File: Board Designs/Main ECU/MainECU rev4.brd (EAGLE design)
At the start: 120.6 x 78.9 mm, 155 parts, among them Q1 MMBT3904LT3G, Q11 MMBT3904LT3G, Q2 MMBT3904LT3G, Q3 MMBT3904LT3G, Q4 MMBT3904LT3G, Q5 MMBT3904LT3G, Q6 MMBT3904LT3G, Q7 MMBT3904LT3G, Q8 MMBT3904LT3G, Q9 MMBT3904LT3G, X1 CONNECTOR-37, X2 CONNECTOR-4AUTOSPORT, X3 CONNECTOR-4NANO-FIT-VERTICAL-4, X4 CONNECTOR-4NANO-FIT-VERTICAL-4

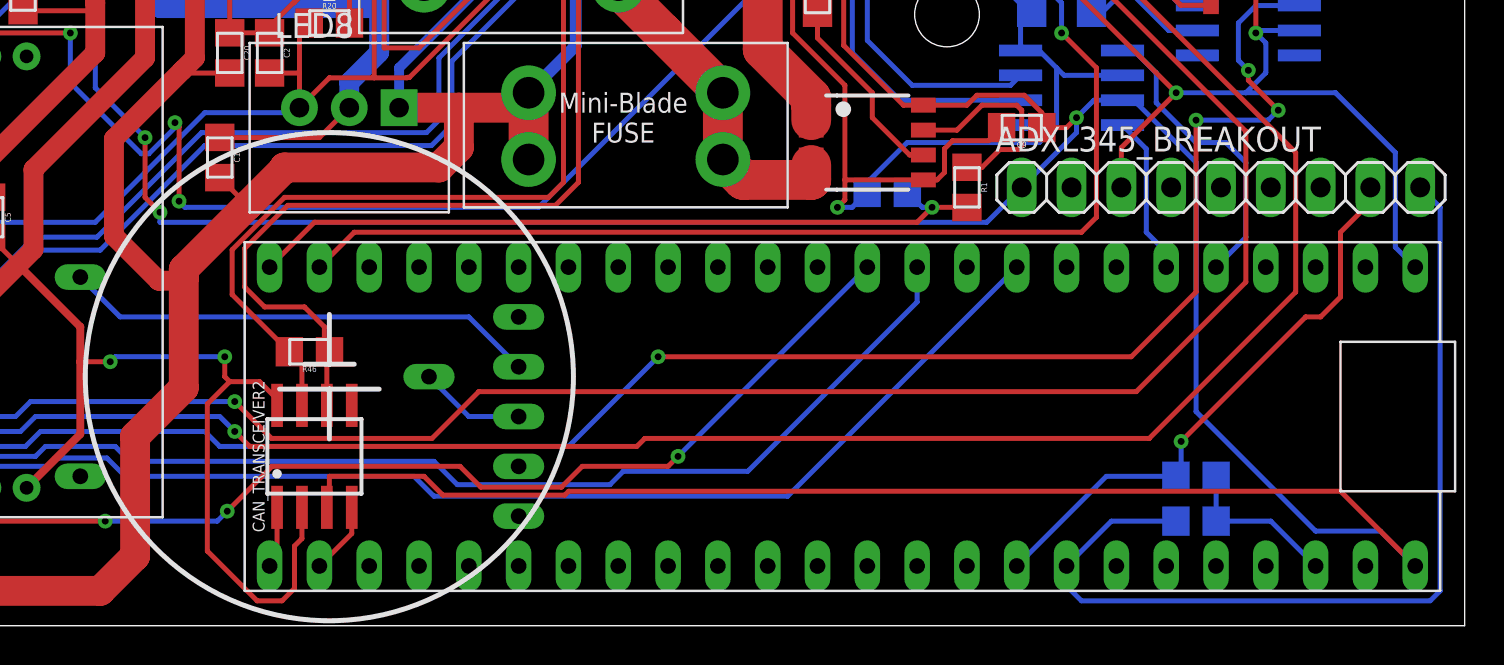
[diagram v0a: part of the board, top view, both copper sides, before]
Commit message: Main ECU rev4: Fixed filter capacitor values again, added filters to current sensor outputs
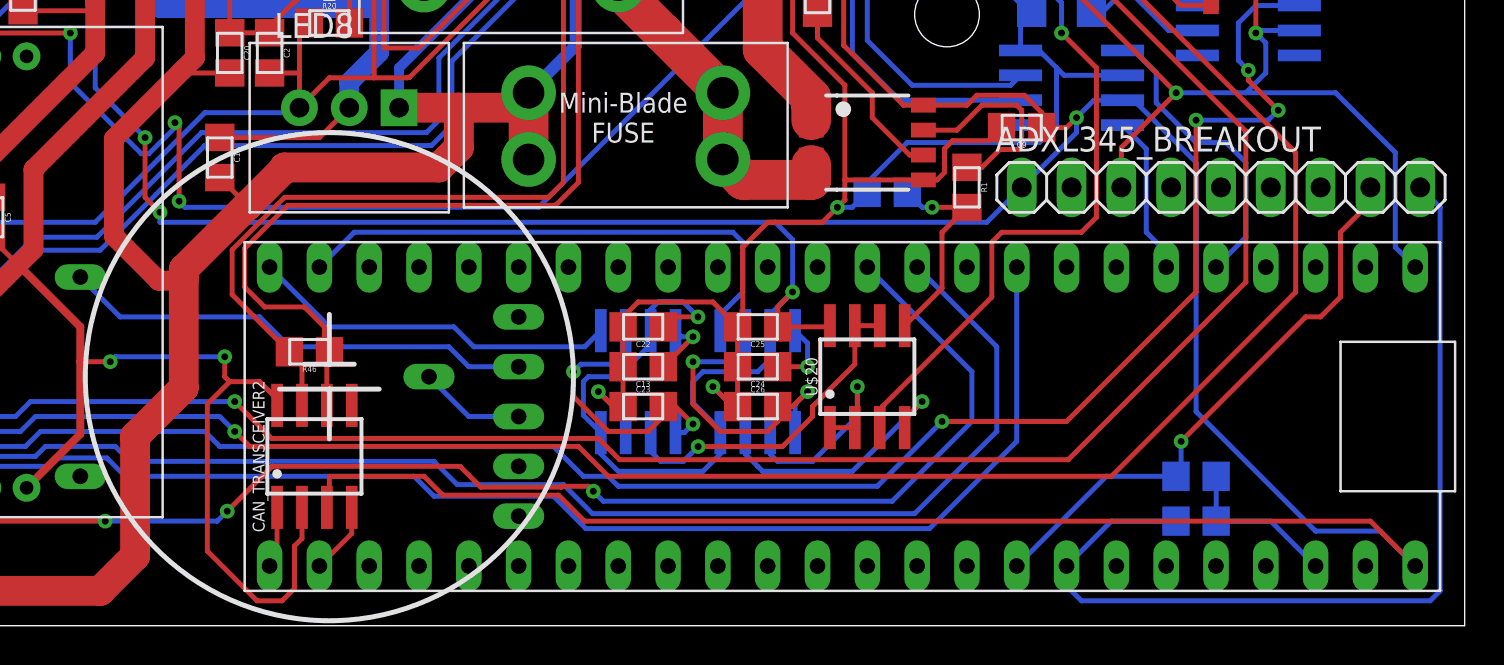
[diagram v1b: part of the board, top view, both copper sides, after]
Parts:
- added C13, C24: 470pF, HyTechDevices:0805
- added C22, C23, C25, C26: .1uF, HyTechDevices:0805
- added U$20: MCP6002SOIC, HyTechDevices:SOIC-08
- added U$21, U$22: (no value), HyTechDevices:SOIC-08
- C14, C17, C3: value 47pF -> 47nF
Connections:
- new net COOLINGSENSE_FILT: U$2.A12, U$22.5
- new net ECUSENSE_FILT: U$2.A13, U$21.5
- new net N$20: U$20.1, U$20.2, U$22.2
- new net N$39: U$20.6, U$20.7, U$21.2
- new net N$43: C23.2, U$21.1, U$21.6
- new net N$44: C13.1, U$21.8
- new net N$67: C26.2, U$22.1, U$22.6
- new net N$68: C24.1, U$22.8
- net COOLINGSENSE: now also U$20.3; no longer U$2.A12
- net ECUSENSE: now also U$20.5; no longer U$2.A13
- net GND: now also C13.2, C22.2, C23.1, C24.2, C25.2, C26.1, U$20.4, U$21.3, U$22.3
- net TELEMETRY5V: now also C22.1, C25.1, U$20.8, U$21.4, U$21.7, U$22.4, U$22.7
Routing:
- net GND: track 774.4 -> 822.2 mm, vias 25 -> 28
- net TELEMETRY5V: track 245.3 -> 288.2 mm, vias 5 -> 7
- net ECUSENSE: track 38.4 -> 10.7 mm
- net COOLINGSENSE_FILT: track 0.00 -> 27.5 mm
- net COOLINGSENSE: track 57.5 -> 34.6 mm
- net ECUSENSE_FILT: track 0.00 -> 18.9 mm
- net N$39: track 0.00 -> 17.2 mm, vias 0 -> 1
- net N$67: track 0.00 -> 16.2 mm, vias 0 -> 2
- net N$43: track 0.00 -> 14.6 mm, vias 0 -> 2
- net XBDI: track 63.8 -> 76.6 mm
- net N$20: track 0.00 -> 11.6 mm, vias 0 -> 1
- net XBDO: track 68.7 -> 79.6 mm
- net XB8: track 68.8 -> 75.3 mm
- net N$68: track 0.00 -> 3.62 mm, vias 0 -> 1
- net N$44: track 0.00 -> 3.17 mm, vias 0 -> 1
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
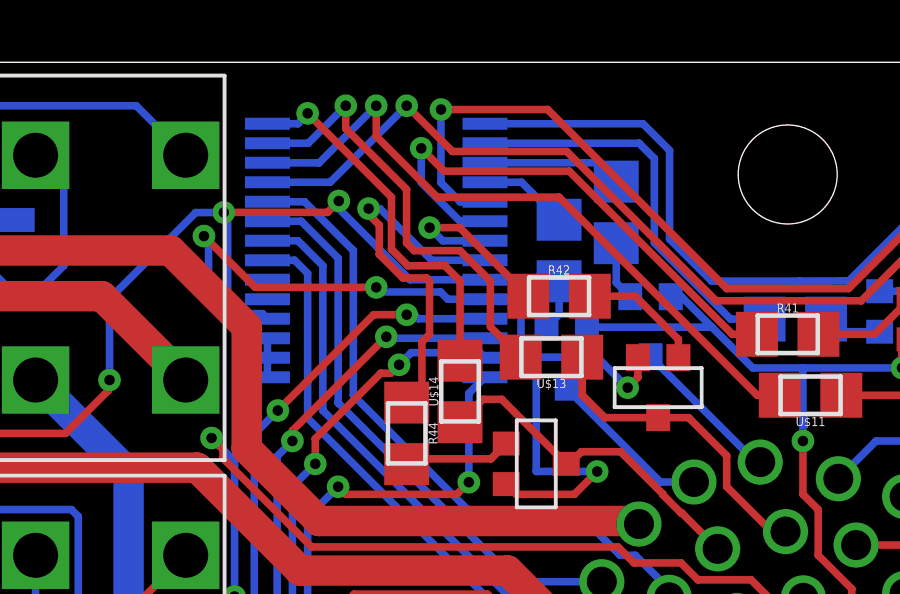
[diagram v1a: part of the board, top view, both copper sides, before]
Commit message: Main ECU rev2/4: Add brake light NPN p/n
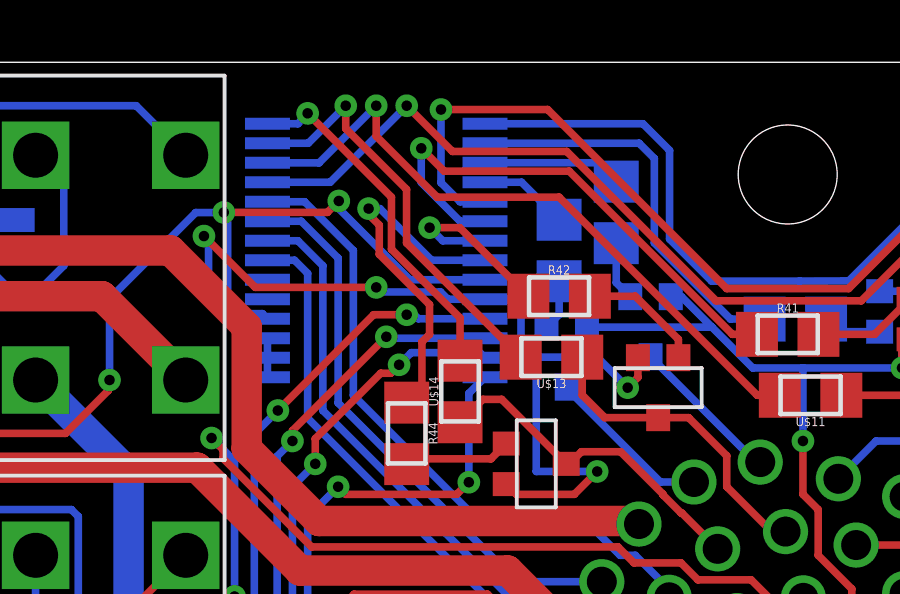
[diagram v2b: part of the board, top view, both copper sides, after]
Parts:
- Q10: value (none) -> MMBT3904LT3G
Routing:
- net DASH_CTRL7_IN: track 14.8 -> 13.9 mm
- net DASH_CTRL8_IN: track 12.6 -> 11.8 mm
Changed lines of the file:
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@@
 <attribute name="VALUE" x="59.6392" y="67.945" size="0.3048" layer="27" rot="R90" align="top-center"/>
 </element>
-<element name="Q10" library="HyTechDevices" package="SOT23" value="" x="59.182" y="49.022" smashed="yes" rot="MR0"/>
+<element name="Q10" library="HyTechDevices" package="SOT23" value="MMBT3904LT3G" x="59.182" y="49.022" smashed="yes" rot="MR0"/>
 <element name="U$15" library="HyTechDevices" package="SOT23" value="BJT_PNPSOT" x="58.928" y="54.61" smashed="yes" rot="MR90"/>
 <element name="R10" library="HyTechDevices" package="0805" value="2.2k" x="64.262" y="46.228" smashed="yes">
@@
 <wire x1="55.88" y1="74.041" x2="56.259" y2="74.041" width="0.254" layer="16"/>
 <wire x1="57.658" y1="69.596" x2="57.658" y2="68.081" width="0.254" layer="1"/>
-<wire x1="57.912" y1="71.628" x2="57.912" y2="69.85" width="0.254" layer="1"/>
 <wire x1="57.912" y1="69.85" x2="57.658" y2="69.596" width="0.254" layer="1"/>
 <wire x1="56.259" y1="74.041" x2="57.981" y2="72.319" width="0.254" layer="16"/>
@@
 <wire x1="55.88" y1="73.8472625" x2="56.2356" y2="73.4916625" width="0.254" layer="1"/>
 <wire x1="56.2356" y1="73.4916625" x2="56.2356" y2="72.51665" width="0.254" layer="1"/>
-<wire x1="56.2356" y1="72.51665" x2="57.02265" y2="71.7296" width="0.254" layer="1"/>
-<wire x1="57.02265" y1="71.7296" x2="57.8104" y2="71.7296" width="0.254" layer="1"/>
-<wire x1="57.8104" y1="71.7296" x2="57.912" y2="71.628" width="0.254" layer="1"/>
 <wire x1="57.981" y1="72.319" x2="59.759" y2="72.319" width="0.254" layer="16"/>
 <wire x1="55.88" y1="74.041" x2="55.88" y2="73.8472625" width="0.254" layer="1"/>
+<wire x1="56.2356" y1="72.51665" x2="57.912" y2="70.84025" width="0.254" layer="1"/>
+<wire x1="57.912" y1="70.84025" x2="57.912" y2="69.85" width="0.254" layer="1"/>
 </signal>
 <signal name="DASH_CTRL7_OUT">
@@
 <contactref element="U$13" pad="2"/>
 <contactref element="U$17" pad="27"/>
-<wire x1="57.1455" y1="72.8935" x2="57.3995" y2="72.6395" width="0.254" layer="1"/>
 <via x="55.118" y="77.47" extent="1-16" drill="0.35"/>
-<wire x1="59.9395" y1="70.0995" x2="60.951" y2="69.088" width="0.254" layer="1"/>
 <wire x1="55.118" y1="77.47" x2="53.867" y2="76.219" width="0.254" layer="16"/>
 <wire x1="53.867" y1="76.219" x2="52.509" y2="76.219" width="0.254" layer="16"/>
 <wire x1="57.1455" y1="74.6805" x2="57.1455" y2="72.8935" width="0.254" layer="1"/>
-<wire x1="57.3995" y1="72.6395" x2="58.928" y2="72.6395" width="0.254" layer="1"/>
 <wire x1="55.118" y1="76.708" x2="57.1455" y2="74.6805" width="0.254" layer="1"/>
 <wire x1="55.118" y1="77.47" x2="55.118" y2="76.708" width="0.254" layer="1"/>
-<wire x1="58.928" y1="72.6395" x2="59.9395" y2="71.628" width="0.254" layer="1"/>
-<wire x1="59.9395" y1="71.628" x2="59.9395" y2="70.0995" width="0.254" layer="1"/>
+<wire x1="57.1455" y1="72.8935" x2="60.951" y2="69.088" width="0.254" layer="1"/>
 </signal>
 <signal name="DASH_CTRL6_IN">
@@
 <via x="53.848" y="77.216" extent="1-16" drill="0.35"/>
 <wire x1="53.848" y1="77.192" x2="53.525" y2="76.869" width="0.254" layer="16"/>
-<wire x1="56.642" y1="72.6849875" x2="56.642" y2="74.422" width="0.254" layer="1"/>
-<wire x1="57.1909875" y1="72.136" x2="58.42" y2="72.136" width="0.254" layer="1"/>
-<wire x1="57.1909875" y1="72.136" x2="56.642" y2="72.6849875" width="0.254" layer="1"/>
+<wire x1="56.642" y1="74.422" x2="56.642" y2="72.6849875" width="0.254" layer="1"/>
 <wire x1="53.848" y1="77.216" x2="56.642" y2="74.422" width="0.254" layer="1"/>
 <wire x1="53.848" y1="77.216" x2="53.848" y2="77.192" width="0.254" layer="16"/>
 <wire x1="53.525" y1="76.869" x2="52.509" y2="76.869" width="0.254" layer="16"/>
-<wire x1="58.42" y1="72.136" x2="58.928" y2="71.628" width="0.254" layer="1"/>
-<wire x1="58.928" y1="71.628" x2="58.928" y2="68.97" width="0.254" layer="1"/>
+<wire x1="56.642" y1="72.6849875" x2="58.928" y2="70.3989875" width="0.254" layer="1"/>
+<wire x1="58.928" y1="70.3989875" x2="58.928" y2="68.97" width="0.254" layer="1"/>
 </signal>
 <signal name="N$28">

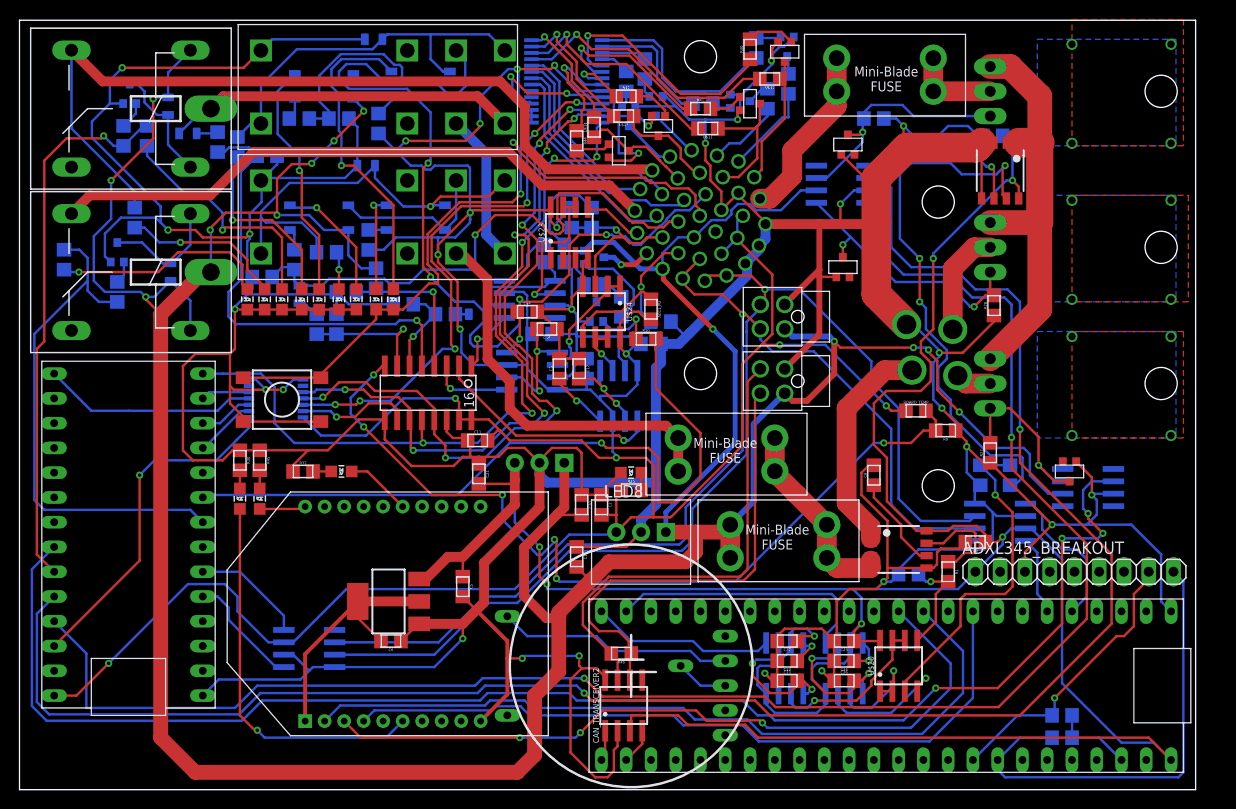
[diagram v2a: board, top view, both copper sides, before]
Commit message: Main ECU rev3/4: Update silkscreen for manufacturing, Main ECU rev4: switch to high-side dashboard switching and flip parts on wrong side
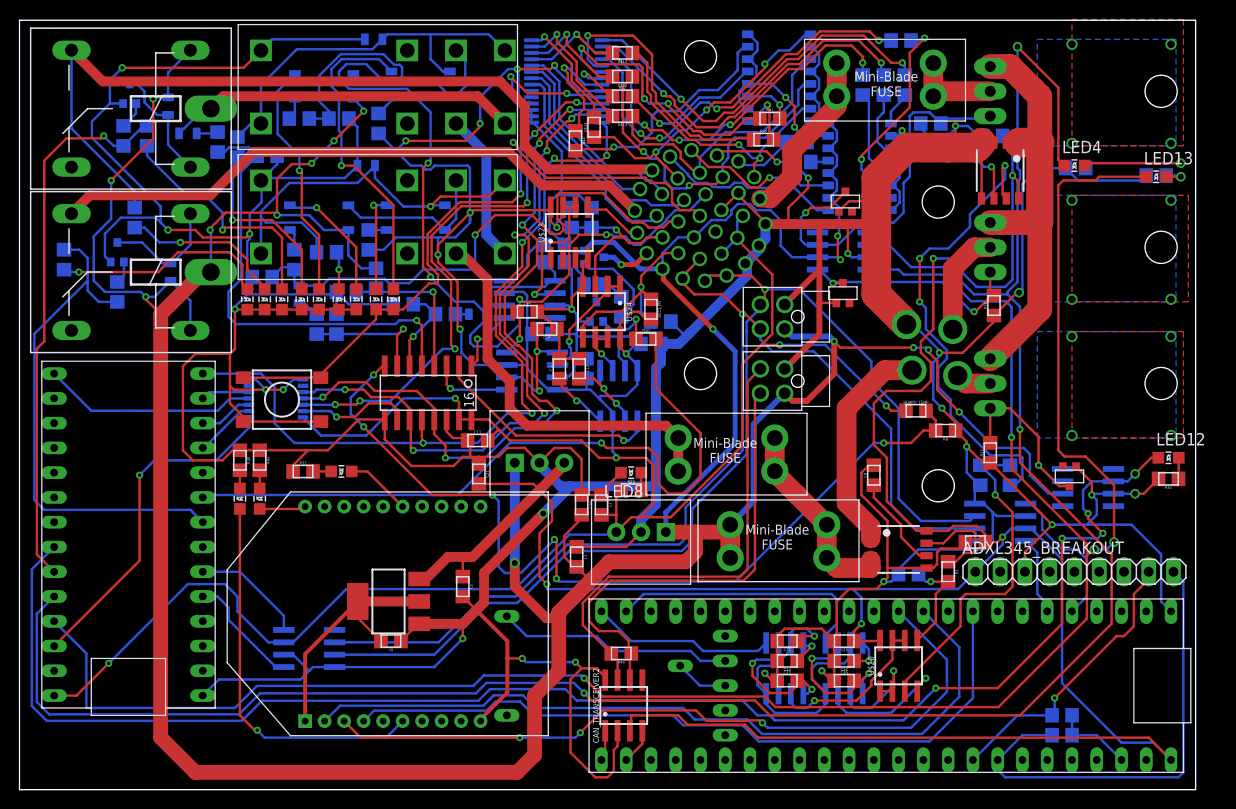
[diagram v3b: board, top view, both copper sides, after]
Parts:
- removed Q1, Q2, Q3, Q4, Q5, Q6, Q7, Q8: MMBT3904LT3G, HyTechDevices:SOT23
- added LED12, LED13, LED4: Red, HyTechDevices:LED-805
- added R25, R51, R52: 100, HyTechDevices:0805
- added U$29, U$30: TLP291-4, HyTechDevices:11-11F1
- moved R39 28.5 mm to (90.4, 76.8), turned to 180 degrees
- moved R38 22.4 mm to (86.5, 72.3)
- moved R36 18.6 mm to (88.6, 72.3), turned to 270 degrees
- moved R35 15.7 mm to (90.8, 72.3), turned to 270 degrees
- moved U$12 15.3 mm to (61.8, 75.6)
- moved U$11 10.3 mm to (61.8, 73.2)
- moved R40 9.38 mm to (76.3, 66.7), turned to 0 degrees
- moved R37 7.33 mm to (80.1, 64.4), turned to 0 degrees
- moved R41 7.18 mm to (77.0, 68.8)
- moved U$5 6.86 mm to (84.5, 55.2)
- moved R43 6.03 mm to (79.8, 66.4), turned to 0 degrees
- moved R24 5.86 mm to (93.5, 68.3), turned to 180 degrees
- moved D8 5.85 mm to (84.7, 60.3)
- moved D7 2.67 mm to (84.5, 50.9)
- moved D9 0.51 mm to (107.7, 32.1)
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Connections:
- new net N$69: LED4.C, R25.1
- new net N$70: LED12.C, R51.1
- new net N$71: LED13.C, R52.1
- net +12V: now also U$29.10, U$29.12, U$29.14, U$29.16, U$30.10, U$30.12, U$30.14, U$30.16
- net DASH_IO3: now also U$29.11; no longer Q3.3
- net DASH_IO4: now also U$29.9; no longer Q4.3
- net DASH_IO5: now also U$30.15; no longer Q5.3
- net DASH_IO6: now also U$30.13; no longer Q6.3
- net DASH_IO7: now also U$30.11; no longer Q7.3
- net DASH_IO8: now also U$30.9; no longer Q8.3
- net FAN1CONTROL: now also LED4.A
- net FAN2CONTROL: now also LED13.A
- net GND: now also R25.2, R51.2, R52.2, U$29.2, U$29.4, U$29.6, U$29.8, U$30.2, U$30.4, U$30.6, U$30.8; no longer Q1.2, Q2.2, Q3.2, Q4.2, Q5.2, Q6.2, Q7.2, Q8.2
- net N$30: now also U$29.3; no longer Q2.1
- net N$42: now also U$29.13; no longer Q2.3
- net N$51: now also U$29.1; no longer Q1.1
- net N$52: now also U$29.5; no longer Q3.1
- net N$53: now also U$29.7; no longer Q4.1
- net N$54: now also U$30.1; no longer Q5.1
- net N$55: now also U$30.3; no longer Q6.1
- net N$56: now also U$30.5; no longer Q7.1
- net N$57: now also U$30.7; no longer Q8.1
- net N$59: now also U$29.15; no longer Q1.3
- net PUMPCONTROL: now also LED12.A
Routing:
- net FAN2CONTROL: track 175.8 -> 223.7 mm, vias 2 -> 4
- net DASH_CTRL4: track 2.99 -> 41.2 mm, vias 0 -> 4
- net +12V: track 381.7 -> 419.0 mm, vias 13 -> 16
- net DASH_CTRL3: track 4.64 -> 39.4 mm, vias 0 -> 4
- net FAN1CONTROL: track 190.1 -> 223.7 mm, vias 2 -> 3
- net DASH_CTRL2: track 13.4 -> 38.3 mm, vias 0 -> 2
- net GND: track 822.2 -> 845.5 mm, vias 28 -> 30
- net DASH_IO6: track 14.2 -> 35.7 mm, vias 0 -> 2
- net DASH_IO8: track 11.3 -> 32.2 mm, vias 0 -> 3
- net N$57: track 3.60 -> 24.1 mm, vias 0 -> 1
- net N$53: track 1.71 -> 21.9 mm, vias 0 -> 2
- net N$69: track 0.00 -> 19.9 mm, vias 0 -> 1
- net DASH_CTRL1: track 21.1 -> 40.4 mm, vias 0 -> 2
- net DASH_IO7: track 10.5 -> 29.5 mm
- net DASH_CTRL5_IN: track 28.0 -> 10.2 mm
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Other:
- board text added: "HyTech 2019 Main ECU rev4"
- board text removed: "HyTech 2019 Main ECU rev3"
